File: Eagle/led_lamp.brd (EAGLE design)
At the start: 100 x 80 mm, 7 parts

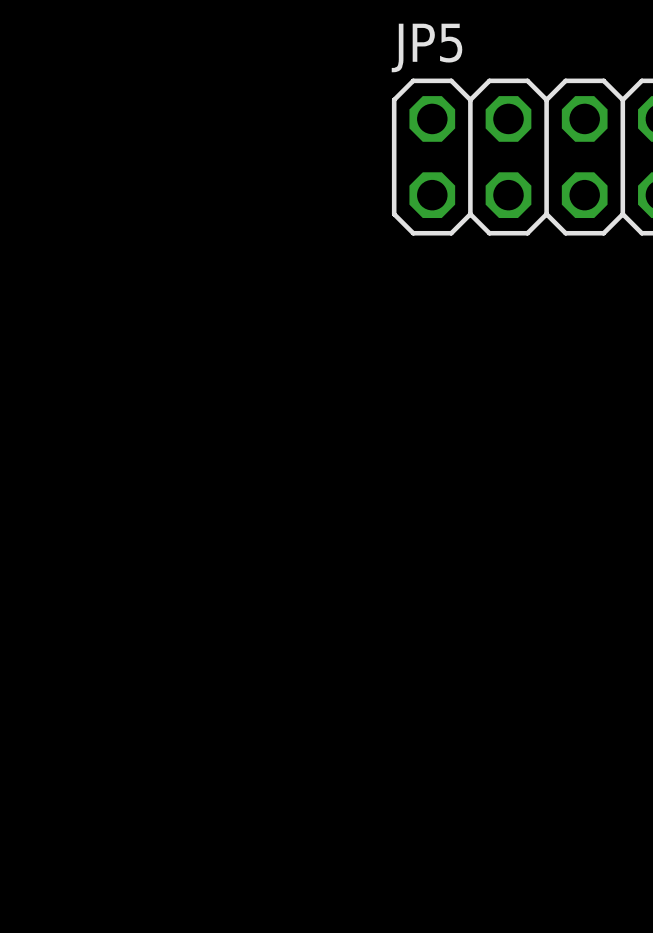
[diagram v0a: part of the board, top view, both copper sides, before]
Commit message: Updated arduino project and eagle project
Eagle:
- Added push button along with auxiliary componetns

Arduino Project
- Added profiles
- Added serial command to set both LEDs with one command
- Merged seperate set_led functions into one
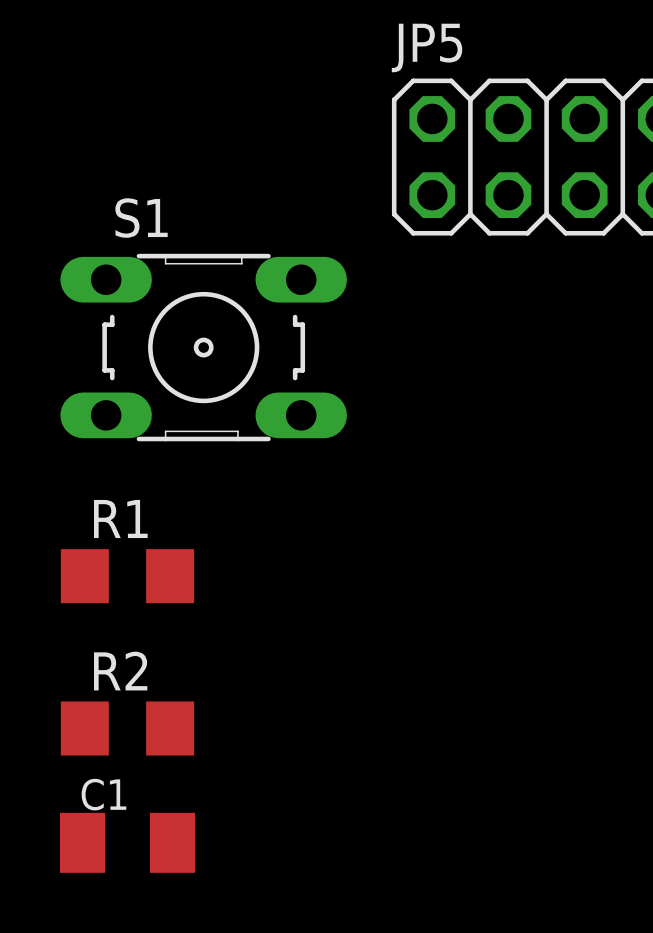
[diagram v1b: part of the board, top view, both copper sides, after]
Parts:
- added C1: 0.1uF, rcl:C1206K
- added R1: 10k, rcl:R1206
- added R2: 100k, rcl:R1206
- added S1: (no value), switch-omron:B3F-10XX
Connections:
- new net 3.3V: C1.1, JP1.2, S1.2
- new net N$1: R1.1, R2.2, S1.4
- new net N$2: C1.2, JP2.8, R1.2
- net GND: now also R2.1
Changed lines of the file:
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@@
 <layers>
 <layer number="1" name="Top" color="4" fill="1" visible="yes" active="yes"/>
+<layer number="2" name="Route2" color="1" fill="3" visible="no" active="no"/>
+<layer number="3" name="Route3" color="4" fill="3" visible="no" active="no"/>
+<layer number="4" name="Route4" color="1" fill="4" visible="no" active="no"/>
+<layer number="5" name="Route5" color="4" fill="4" visible="no" active="no"/>
+<layer number="6" name="Route6" color="1" fill="8" visible="no" active="no"/>
+<layer number="7" name="Route7" color="4" fill="8" visible="no" active="no"/>
+<layer number="8" name="Route8" color="1" fill="2" visible="no" active="no"/>
+<layer number="9" name="Route9" color="4" fill="2" visible="no" active="no"/>
+<layer number="10" name="Route10" color="1" fill="7" visible="no" active="no"/>
+<layer number="11" name="Route11" color="4" fill="7" visible="no" active="no"/>
+<layer number="12" name="Route12" color="1" fill="5" visible="no" active="no"/>
+<layer number="13" name="Route13" color="4" fill="5" visible="no" active="no"/>
+<layer number="14" name="Route14" color="1" fill="6" visible="no" active="no"/>
+<layer number="15" name="Route15" color="4" fill="6" visible="no" active="no"/>
 <layer number="16" name="Bottom" color="1" fill="1" visible="yes" active="yes"/>
 <layer number="17" name="Pads" color="2" fill="1" visible="yes" active="yes"/>
@@
 <attribute name="VALUE" x="-34.29" y="-15.875" size="1.27" layer="27"/>
 </element>
+<element name="S1" library="switch-omron" library_urn="urn:adsk.eagle:library:377" package="B3F-10XX" package3d_urn="urn:adsk.eagle:package:27496/1" value="" x="-40.64" y="-17.78" smashed="yes">
+<attribute name="MF" value="" x="-40.64" y="-17.78" size="1.778" layer="27" display="off"/>
+<attribute name="MPN" value="B3F-1000" x="-40.64" y="-17.78" size="1.778" layer="27" display="off"/>
+<attribute name="NAME" x="-43.688" y="-14.097" size="1.27" layer="25" ratio="10"/>
+<attribute name="OC_FARNELL" value="176432" x="-40.64" y="-17.78" size="1.778" layer="27" display="off"/>
+<attribute name="OC_NEWARK" value="36M3542" x="-40.64" y="-17.78" size="1.778" layer="27" display="off"/>
+<attribute name="VALUE" x="-43.688" y="-22.86" size="1.27" layer="27" ratio="10"/>
+</element>
+<element name="R1" library="rcl" library_urn="urn:adsk.eagle:library:334" package="R1206" package3d_urn="urn:adsk.eagle:package:23540/2" value="10k" x="-43.18" y="-25.4" smashed="yes">
+<attribute name="NAME" x="-44.45" y="-24.13" size="1.27" layer="25"/>
+<attribute name="SPICEPREFIX" value="R" x="-43.18" y="-25.4" size="1.778" layer="27" display="off"/>
+<attribute name="VALUE" x="-44.45" y="-27.94" size="1.27" layer="27"/>
+</element>
+<element name="R2" library="rcl" library_urn="urn:adsk.eagle:library:334" package="R1206" package3d_urn="urn:adsk.eagle:package:23540/2" value="100k" x="-43.18" y="-30.48" smashed="yes">
+<attribute name="NAME" x="-44.45" y="-29.21" size="1.27" layer="25"/>
+<attribute name="SPICEPREFIX" value="R" x="-43.18" y="-30.48" size="1.778" layer="27" display="off"/>
+<attribute name="VALUE" x="-44.45" y="-33.02" size="1.27" layer="27"/>
+</element>
+<element name="C1" library="rcl" library_urn="urn:adsk.eagle:library:334" package="C1206K" package3d_urn="urn:adsk.eagle:package:23682/2" value="0.1uF" x="-43.18" y="-34.29" smashed="yes">
+<attribute name="NAME" x="-44.78" y="-33.19" size="1.016" layer="25"/>
+<attribute name="SPICEPREFIX" value="C" x="-43.18" y="-34.29" size="1.778" layer="27" display="off"/>
+<attribute name="VALUE" x="-44.78" y="-36.39" size="1.016" layer="27"/>
+</element>
 </elements>
 <signals>
@@
 <contactref element="JP1" pad="6"/>
 <contactref element="JP1" pad="7"/>
+<contactref element="R2" pad="1"/>
+<wire x1="-27.94" y1="-3.81" x2="-44.602" y2="-30.48" width="0" layer="19" extent="1-1"/>
 <wire x1="-20.32" y1="19.05" x2="-27.94" y2="-3.81" width="0" layer="19" extent="1-1"/>
 <wire x1="-17.78" y1="19.05" x2="-20.32" y2="19.05" width="0" layer="19" extent="1-1"/>
@@
 <wire x1="-20.32" y1="-12.7" x2="-30.48" y2="-3.81" width="0" layer="19" extent="1-1"/>
 </signal>
+<signal name="N$1">
+<contactref element="S1" pad="4"/>
+<contactref element="R1" pad="1"/>
+<contactref element="R2" pad="2"/>
+<wire x1="-44.602" y1="-25.4" x2="-41.758" y2="-30.48" width="0" layer="19" extent="1-1"/>
+<wire x1="-37.3888" y1="-20.0406" x2="-44.602" y2="-25.4" width="0" layer="19" extent="1-1"/>
+</signal>
+<signal name="N$2">
+<contactref element="R1" pad="2"/>
+<contactref element="C1" pad="2"/>
+<contactref element="JP2" pad="8"/>
+<wire x1="-41.758" y1="-25.4" x2="-41.68" y2="-34.29" width="0" layer="19" extent="1-1"/>
+<wire x1="-25.4" y1="5.08" x2="-41.758" y2="-25.4" width="0" layer="19" extent="1-1"/>
+</signal>
+<signal name="3.3V">
+<contactref element="S1" pad="2"/>
+<contactref element="C1" pad="1"/>
+<contactref element="JP1" pad="2"/>
+<wire x1="-37.3888" y1="-15.5194" x2="-44.68" y2="-34.29" width="0" layer="19" extent="1-1"/>
+<wire x1="-30.48" y1="19.05" x2="-37.3888" y2="-15.5194" width="0" layer="19" extent="1-1"/>
+</signal>
 </signals>

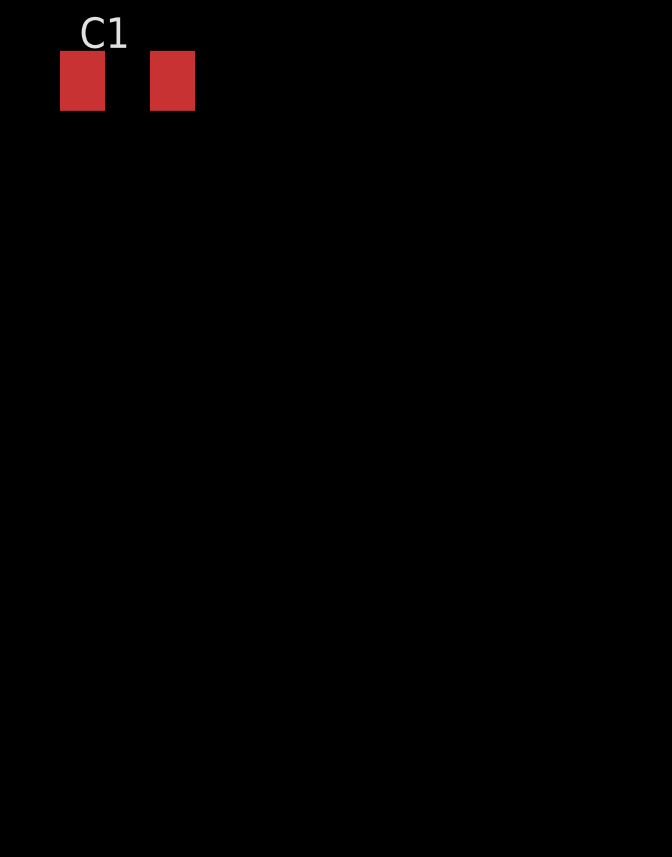
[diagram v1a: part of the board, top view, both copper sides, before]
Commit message: Added pwr button to eagle pcb
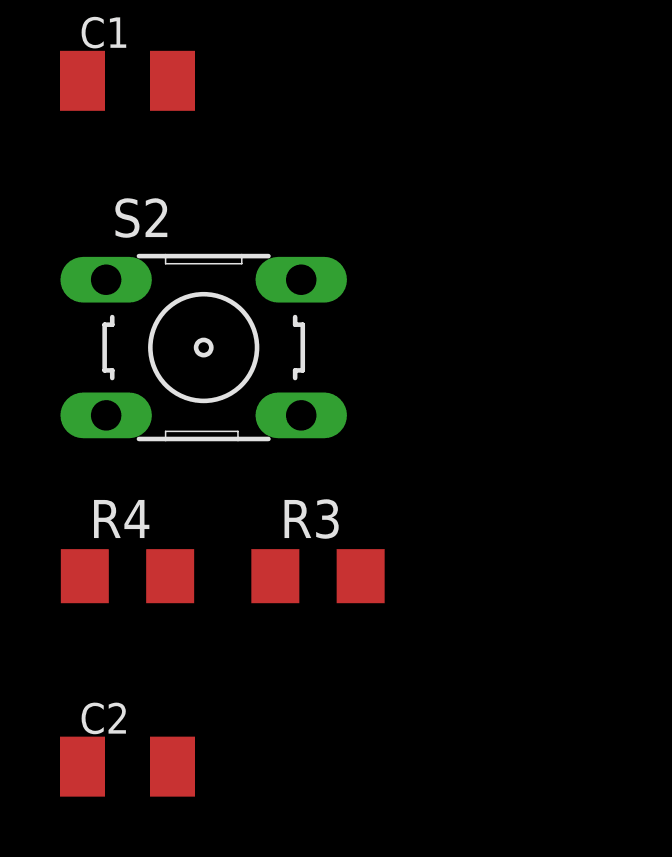
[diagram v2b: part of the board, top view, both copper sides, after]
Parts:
- added C2: 0.1uF, rcl:C1206K
- added R3: 10k, rcl:R1206
- added R4: 100k, rcl:R1206
- added S2: (no value), switch-omron:B3F-10XX
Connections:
- removed net 3.3V: C1.1, JP1.2, S1.2
- new net 3.3V1: C1.1, C2.1, JP1.2, S1.2, S2.2
- new net N$3: R3.1, R4.2, S2.4
- new net N$4: C2.2, JP2.10, R3.2
- net GND: now also R4.1
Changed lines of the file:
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@@
 <attribute name="VALUE" x="-44.78" y="-36.39" size="1.016" layer="27"/>
+</element>
+<element name="S2" library="switch-omron" library_urn="urn:adsk.eagle:library:377" package="B3F-10XX" package3d_urn="urn:adsk.eagle:package:27496/1" value="" x="-40.64" y="-43.18" smashed="yes">
+<attribute name="MF" value="" x="-50.8" y="-30.48" size="1.778" layer="27" display="off"/>
+<attribute name="MPN" value="B3F-1000" x="-50.8" y="-30.48" size="1.778" layer="27" display="off"/>
+<attribute name="NAME" x="-43.688" y="-39.497" size="1.27" layer="25" ratio="10"/>
+<attribute name="OC_FARNELL" value="176432" x="-50.8" y="-30.48" size="1.778" layer="27" display="off"/>
+<attribute name="OC_NEWARK" value="36M3542" x="-50.8" y="-30.48" size="1.778" layer="27" display="off"/>
+<attribute name="VALUE" x="-43.688" y="-48.26" size="1.27" layer="27" ratio="10"/>
+</element>
+<element name="R3" library="rcl" library_urn="urn:adsk.eagle:library:334" package="R1206" package3d_urn="urn:adsk.eagle:package:23540/2" value="10k" x="-36.83" y="-50.8" smashed="yes">
+<attribute name="NAME" x="-38.1" y="-49.53" size="1.27" layer="25"/>
+<attribute name="SPICEPREFIX" value="R" x="-53.34" y="-40.64" size="1.778" layer="27" display="off"/>
+<attribute name="VALUE" x="-38.1" y="-53.34" size="1.27" layer="27"/>
+</element>
+<element name="R4" library="rcl" library_urn="urn:adsk.eagle:library:334" package="R1206" package3d_urn="urn:adsk.eagle:package:23540/2" value="100k" x="-43.18" y="-50.8" smashed="yes">
+<attribute name="NAME" x="-44.45" y="-49.53" size="1.27" layer="25"/>
+<attribute name="SPICEPREFIX" value="R" x="-53.34" y="-46.99" size="1.778" layer="27" display="off"/>
+<attribute name="VALUE" x="-44.45" y="-53.34" size="1.27" layer="27"/>
+</element>
+<element name="C2" library="rcl" library_urn="urn:adsk.eagle:library:334" package="C1206K" package3d_urn="urn:adsk.eagle:package:23682/2" value="0.1uF" x="-43.18" y="-57.15" smashed="yes">
+<attribute name="NAME" x="-44.78" y="-56.05" size="1.016" layer="25"/>
+<attribute name="SPICEPREFIX" value="C" x="-53.34" y="-53.34" size="1.778" layer="27" display="off"/>
+<attribute name="VALUE" x="-44.78" y="-59.25" size="1.016" layer="27"/>
 </element>
 </elements>
@@
 <contactref element="JP1" pad="7"/>
 <contactref element="R2" pad="1"/>
+<contactref element="R4" pad="1"/>
+<wire x1="-44.602" y1="-30.48" x2="-44.602" y2="-50.8" width="0" layer="19" extent="1-1"/>
 <wire x1="-27.94" y1="-3.81" x2="-44.602" y2="-30.48" width="0" layer="19" extent="1-1"/>
 <wire x1="-20.32" y1="19.05" x2="-27.94" y2="-3.81" width="0" layer="19" extent="1-1"/>
@@
 <wire x1="-25.4" y1="5.08" x2="-41.758" y2="-25.4" width="0" layer="19" extent="1-1"/>
 </signal>
-<signal name="3.3V">
+<signal name="N$3">
+<contactref element="S2" pad="4"/>
+<contactref element="R3" pad="1"/>
+<contactref element="R4" pad="2"/>
+<wire x1="-38.252" y1="-50.8" x2="-41.758" y2="-50.8" width="0" layer="19" extent="1-1"/>
+<wire x1="-37.3888" y1="-45.4406" x2="-38.252" y2="-50.8" width="0" layer="19" extent="1-1"/>
+</signal>
+<signal name="N$4">
+<contactref element="R3" pad="2"/>
+<contactref element="C2" pad="2"/>
+<contactref element="JP2" pad="10"/>
+<wire x1="-35.408" y1="-50.8" x2="-41.68" y2="-57.15" width="0" layer="19" extent="1-1"/>
+<wire x1="-22.86" y1="5.08" x2="-35.408" y2="-50.8" width="0" layer="19" extent="1-1"/>
+</signal>
+<signal name="3.3V1">
+<contactref element="S2" pad="2"/>
+<contactref element="C2" pad="1"/>
 <contactref element="S1" pad="2"/>
 <contactref element="C1" pad="1"/>
 <contactref element="JP1" pad="2"/>
+<wire x1="-37.3888" y1="-40.9194" x2="-44.68" y2="-57.15" width="0" layer="19" extent="1-1"/>
+<wire x1="-44.68" y1="-34.29" x2="-37.3888" y2="-40.9194" width="0" layer="19" extent="1-1"/>
 <wire x1="-37.3888" y1="-15.5194" x2="-44.68" y2="-34.29" width="0" layer="19" extent="1-1"/>
 <wire x1="-30.48" y1="19.05" x2="-37.3888" y2="-15.5194" width="0" layer="19" extent="1-1"/>
